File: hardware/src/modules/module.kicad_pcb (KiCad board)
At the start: 2 copper layers, 58 x 33.4 mm, 150 parts, among them J1 CONN_01X06, J5 CONN_01X06, U1 VL53L1X

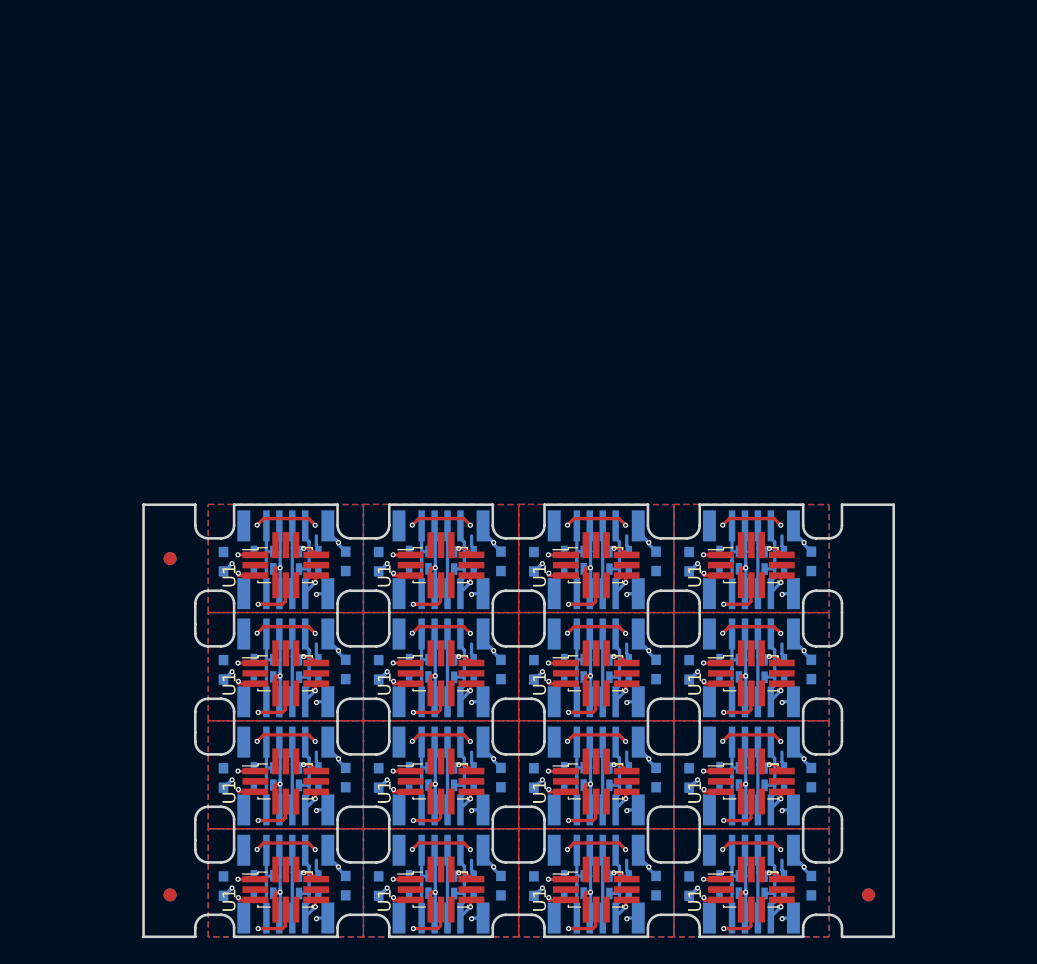
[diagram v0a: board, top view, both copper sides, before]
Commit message: fixed manufactury requirements
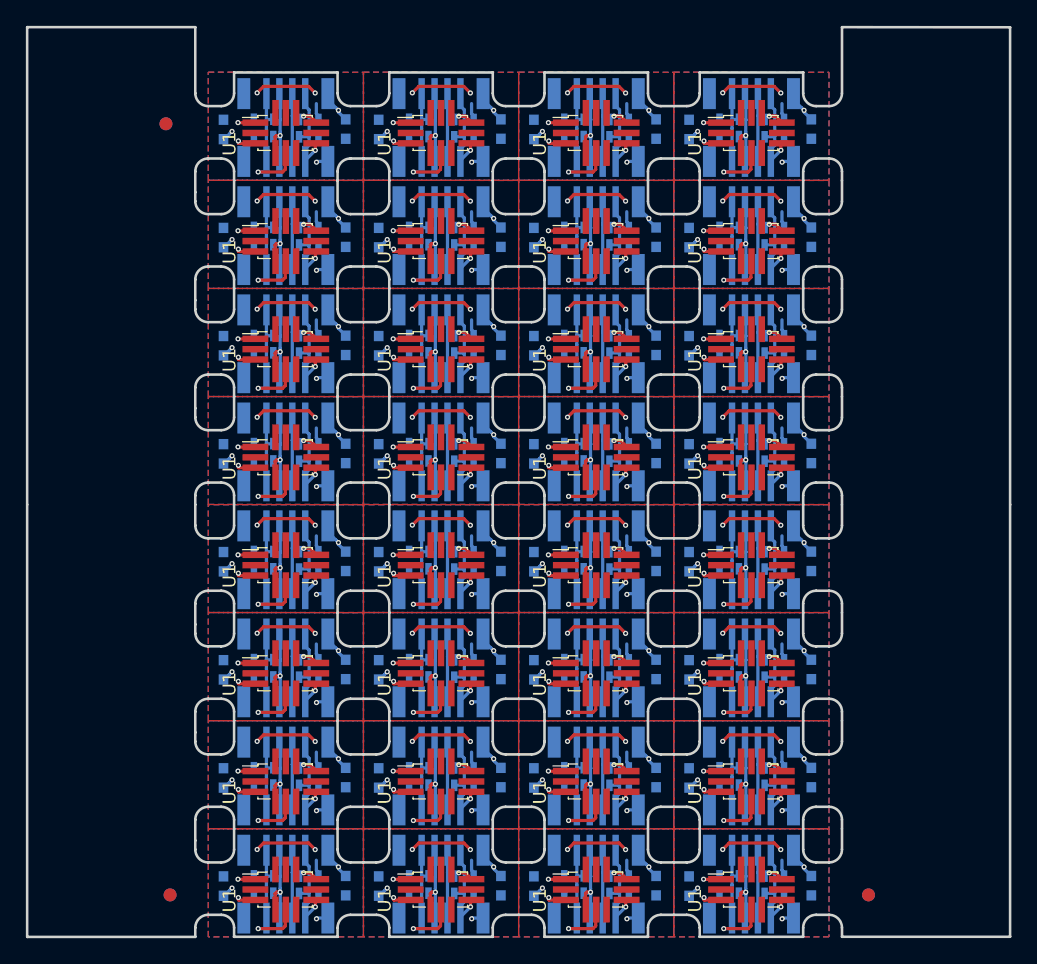
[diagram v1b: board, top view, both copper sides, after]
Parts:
- added C1: 100n, Capacitors_SMD:C_0603, B.Cu at (107.1, 66.9)
- added C1: 100n, Capacitors_SMD:C_0603, B.Cu at (143.1, 50.2)
- added C1: 100n, Capacitors_SMD:C_0603, B.Cu at (131.1, 50.2)
- added C1: 100n, Capacitors_SMD:C_0603, B.Cu at (119.1, 41.8)
- added C1: 100n, Capacitors_SMD:C_0603, B.Cu at (143.1, 66.9)
- added C1: 100n, Capacitors_SMD:C_0603, B.Cu at (143.1, 41.8)
- added C1: 100n, Capacitors_SMD:C_0603, B.Cu at (119.1, 66.9)
- added C1: 100n, Capacitors_SMD:C_0603, B.Cu at (131.1, 66.9)
- added C1: 100n, Capacitors_SMD:C_0603, B.Cu at (107.1, 58.5)
- added C1: 100n, Capacitors_SMD:C_0603, B.Cu at (107.1, 41.8)
- added C1: 100n, Capacitors_SMD:C_0603, B.Cu at (119.1, 58.5)
- added C1: 100n, Capacitors_SMD:C_0603, B.Cu at (131.1, 58.5)
- added C1: 100n, Capacitors_SMD:C_0603, B.Cu at (131.1, 41.8)
- added C1: 100n, Capacitors_SMD:C_0603, B.Cu at (119.1, 50.2)
- added C1: 100n, Capacitors_SMD:C_0603, B.Cu at (143.1, 58.5)
- added C1: 100n, Capacitors_SMD:C_0603, B.Cu at (107.1, 50.2)
- added C2: 4.7u, Capacitors_SMD:C_0603, B.Cu at (128.6, 41.8)
- added C2: 4.7u, Capacitors_SMD:C_0603, B.Cu at (152.6, 41.8)
- added C2: 4.7u, Capacitors_SMD:C_0603, B.Cu at (152.6, 58.5)
- added C2: 4.7u, Capacitors_SMD:C_0603, B.Cu at (152.6, 50.2)
- added C2: 4.7u, Capacitors_SMD:C_0603, B.Cu at (116.6, 66.9)
- added C2: 4.7u, Capacitors_SMD:C_0603, B.Cu at (152.6, 66.9)
- added C2: 4.7u, Capacitors_SMD:C_0603, B.Cu at (140.6, 66.9)
- added C2: 4.7u, Capacitors_SMD:C_0603, B.Cu at (128.6, 66.9)
- added C2: 4.7u, Capacitors_SMD:C_0603, B.Cu at (140.6, 50.2)
- added C2: 4.7u, Capacitors_SMD:C_0603, B.Cu at (128.6, 58.5)
- added C2: 4.7u, Capacitors_SMD:C_0603, B.Cu at (116.6, 41.8)
- added C2: 4.7u, Capacitors_SMD:C_0603, B.Cu at (116.6, 50.2)
- added C2: 4.7u, Capacitors_SMD:C_0603, B.Cu at (116.6, 58.5)
- added C2: 4.7u, Capacitors_SMD:C_0603, B.Cu at (128.6, 50.2)
- added C2: 4.7u, Capacitors_SMD:C_0603, B.Cu at (140.6, 58.5)
- added C2: 4.7u, Capacitors_SMD:C_0603, B.Cu at (140.6, 41.8)
- added J1: CONN_01X06, custom-footprints:CONN_Module, B.Cu at (112.0, 70.1)
- added J1: CONN_01X06, custom-footprints:CONN_Module, B.Cu at (147.9, 45.0)
- added J1: CONN_01X06, custom-footprints:CONN_Module, B.Cu at (135.9, 53.4)
- added J1: CONN_01X06, custom-footprints:CONN_Module, B.Cu at (124.0, 45.0)
- added J1: CONN_01X06, custom-footprints:CONN_Module, B.Cu at (135.9, 45.0)
- added J1: CONN_01X06, custom-footprints:CONN_Module, B.Cu at (135.9, 61.7)
- added J1: CONN_01X06, custom-footprints:CONN_Module, B.Cu at (135.9, 70.1)
- added J1: CONN_01X06, custom-footprints:CONN_Module, B.Cu at (112.0, 45.0)
- added J1: CONN_01X06, custom-footprints:CONN_Module, B.Cu at (147.9, 61.7)
- added J1: CONN_01X06, custom-footprints:CONN_Module, B.Cu at (124.0, 53.4)
- added J1: CONN_01X06, custom-footprints:CONN_Module, B.Cu at (147.9, 70.1)
- added J1: CONN_01X06, custom-footprints:CONN_Module, B.Cu at (124.0, 61.7)
- added J1: CONN_01X06, custom-footprints:CONN_Module, B.Cu at (124.0, 70.1)
- added J1: CONN_01X06, custom-footprints:CONN_Module, B.Cu at (112.0, 53.4)
- added J1: CONN_01X06, custom-footprints:CONN_Module, B.Cu at (147.9, 53.4)
- added J1: CONN_01X06, custom-footprints:CONN_Module, B.Cu at (112.0, 61.7)
- added J5: CONN_01X06, custom-footprints:CONN_Module, B.Cu at (124.0, 56.5)
- added J5: CONN_01X06, custom-footprints:CONN_Module, B.Cu at (112.0, 39.8)
- added J5: CONN_01X06, custom-footprints:CONN_Module, B.Cu at (135.9, 39.8)
- added J5: CONN_01X06, custom-footprints:CONN_Module, B.Cu at (147.9, 56.5)
- added J5: CONN_01X06, custom-footprints:CONN_Module, B.Cu at (147.9, 39.8)
- added J5: CONN_01X06, custom-footprints:CONN_Module, B.Cu at (112.0, 48.1)
- added J5: CONN_01X06, custom-footprints:CONN_Module, B.Cu at (124.0, 48.1)
- added J5: CONN_01X06, custom-footprints:CONN_Module, B.Cu at (135.9, 48.1)
- added J5: CONN_01X06, custom-footprints:CONN_Module, B.Cu at (124.0, 64.8)
- added J5: CONN_01X06, custom-footprints:CONN_Module, B.Cu at (135.9, 64.8)
- added J5: CONN_01X06, custom-footprints:CONN_Module, B.Cu at (112.0, 56.5)
- added J5: CONN_01X06, custom-footprints:CONN_Module, B.Cu at (135.9, 56.5)
- added J5: CONN_01X06, custom-footprints:CONN_Module, B.Cu at (147.9, 64.8)
- added J5: CONN_01X06, custom-footprints:CONN_Module, B.Cu at (112.0, 64.8)
- added J5: CONN_01X06, custom-footprints:CONN_Module, B.Cu at (147.9, 48.1)
- added J5: CONN_01X06, custom-footprints:CONN_Module, B.Cu at (124.0, 39.8)
- added R5: 10k, Resistors_SMD:R_0603, B.Cu at (146.2, 57.8)
- added R5: 10k, Resistors_SMD:R_0603, B.Cu at (146.2, 49.4)
- added R5: 10k, Resistors_SMD:R_0603, B.Cu at (122.2, 41.0)
- added R5: 10k, Resistors_SMD:R_0603, B.Cu at (134.2, 41.0)
- added R5: 10k, Resistors_SMD:R_0603, B.Cu at (134.2, 57.8)
- added R5: 10k, Resistors_SMD:R_0603, B.Cu at (134.2, 49.4)
- added R5: 10k, Resistors_SMD:R_0603, B.Cu at (110.2, 41.0)
- added R5: 10k, Resistors_SMD:R_0603, B.Cu at (110.2, 66.1)
- added R5: 10k, Resistors_SMD:R_0603, B.Cu at (122.2, 66.1)
- added R5: 10k, Resistors_SMD:R_0603, B.Cu at (122.2, 49.4)
- added R5: 10k, Resistors_SMD:R_0603, B.Cu at (146.2, 41.0)
- added R5: 10k, Resistors_SMD:R_0603, B.Cu at (134.2, 66.1)
- added R5: 10k, Resistors_SMD:R_0603, B.Cu at (110.2, 49.4)
- added R5: 10k, Resistors_SMD:R_0603, B.Cu at (146.2, 66.1)
- added R5: 10k, Resistors_SMD:R_0603, B.Cu at (110.2, 57.8)
- added R5: 10k, Resistors_SMD:R_0603, B.Cu at (122.2, 57.8)
- added R6: 10k, Resistors_SMD:R_0603, B.Cu at (146.2, 67.5)
- added R6: 10k, Resistors_SMD:R_0603, B.Cu at (134.2, 50.7)
- added R6: 10k, Resistors_SMD:R_0603, B.Cu at (110.2, 59.1)
- added R6: 10k, Resistors_SMD:R_0603, B.Cu at (110.2, 50.7)
- added R6: 10k, Resistors_SMD:R_0603, B.Cu at (122.2, 59.1)
- added R6: 10k, Resistors_SMD:R_0603, B.Cu at (134.2, 59.1)
- added R6: 10k, Resistors_SMD:R_0603, B.Cu at (146.2, 59.1)
- added R6: 10k, Resistors_SMD:R_0603, B.Cu at (146.2, 42.4)
- added R6: 10k, Resistors_SMD:R_0603, B.Cu at (122.2, 67.5)
- added R6: 10k, Resistors_SMD:R_0603, B.Cu at (134.2, 67.5)
- added R6: 10k, Resistors_SMD:R_0603, B.Cu at (110.2, 67.5)
- added R6: 10k, Resistors_SMD:R_0603, B.Cu at (122.2, 50.7)
- added R6: 10k, Resistors_SMD:R_0603, B.Cu at (134.2, 42.4)
- added R6: 10k, Resistors_SMD:R_0603, B.Cu at (146.2, 50.7)
- added R6: 10k, Resistors_SMD:R_0603, B.Cu at (122.2, 42.4)
- added R6: 10k, Resistors_SMD:R_0603, B.Cu at (110.2, 42.4)
- added R7: 10k, Resistors_SMD:R_0603, B.Cu at (113.7, 66.1)
- added R7: 10k, Resistors_SMD:R_0603, B.Cu at (113.7, 49.4)
- added R7: 10k, Resistors_SMD:R_0603, B.Cu at (149.7, 49.4)
- added R7: 10k, Resistors_SMD:R_0603, B.Cu at (113.7, 41.1)
- added R7: 10k, Resistors_SMD:R_0603, B.Cu at (125.7, 41.1)
- added R7: 10k, Resistors_SMD:R_0603, B.Cu at (137.7, 41.1)
- added R7: 10k, Resistors_SMD:R_0603, B.Cu at (149.7, 41.1)
- added R7: 10k, Resistors_SMD:R_0603, B.Cu at (137.7, 49.4)
- added R7: 10k, Resistors_SMD:R_0603, B.Cu at (149.7, 66.1)
- added R7: 10k, Resistors_SMD:R_0603, B.Cu at (125.7, 49.4)
- added R7: 10k, Resistors_SMD:R_0603, B.Cu at (125.7, 66.1)
- added R7: 10k, Resistors_SMD:R_0603, B.Cu at (149.7, 57.8)
- added R7: 10k, Resistors_SMD:R_0603, B.Cu at (137.7, 57.8)
- added R7: 10k, Resistors_SMD:R_0603, B.Cu at (137.7, 66.1)
- added R7: 10k, Resistors_SMD:R_0603, B.Cu at (125.7, 57.8)
- added R7: 10k, Resistors_SMD:R_0603, B.Cu at (113.7, 57.8)
- added R8: 10k, Resistors_SMD:R_0603, B.Cu at (113.7, 67.5)
- added R8: 10k, Resistors_SMD:R_0603, B.Cu at (137.7, 50.8)
- added R8: 10k, Resistors_SMD:R_0603, B.Cu at (149.7, 67.5)
- added R8: 10k, Resistors_SMD:R_0603, B.Cu at (125.7, 59.1)
- added R8: 10k, Resistors_SMD:R_0603, B.Cu at (137.7, 59.1)
- added R8: 10k, Resistors_SMD:R_0603, B.Cu at (137.7, 42.4)
- added R8: 10k, Resistors_SMD:R_0603, B.Cu at (125.7, 42.4)
- added R8: 10k, Resistors_SMD:R_0603, B.Cu at (149.7, 42.4)
- added R8: 10k, Resistors_SMD:R_0603, B.Cu at (125.7, 67.5)
- added R8: 10k, Resistors_SMD:R_0603, B.Cu at (137.7, 67.5)
- added R8: 10k, Resistors_SMD:R_0603, B.Cu at (149.7, 50.8)
- added R8: 10k, Resistors_SMD:R_0603, B.Cu at (149.7, 59.1)
- added R8: 10k, Resistors_SMD:R_0603, B.Cu at (113.7, 50.8)
- added R8: 10k, Resistors_SMD:R_0603, B.Cu at (113.7, 42.4)
- added R8: 10k, Resistors_SMD:R_0603, B.Cu at (113.7, 59.1)
- added R8: 10k, Resistors_SMD:R_0603, B.Cu at (125.7, 50.8)
- added U1: VL53L1X, custom-footprints:ST_VL53L_HandSoldering, F.Cu at (135.9, 50.5)
- added U1: VL53L1X, custom-footprints:ST_VL53L_HandSoldering, F.Cu at (147.9, 42.1)
- added U1: VL53L1X, custom-footprints:ST_VL53L_HandSoldering, F.Cu at (124.0, 58.9)
- added U1: VL53L1X, custom-footprints:ST_VL53L_HandSoldering, F.Cu at (124.0, 67.2)
- added U1: VL53L1X, custom-footprints:ST_VL53L_HandSoldering, F.Cu at (135.9, 67.2)
- added U1: VL53L1X, custom-footprints:ST_VL53L_HandSoldering, F.Cu at (147.9, 67.2)
- added U1: VL53L1X, custom-footprints:ST_VL53L_HandSoldering, F.Cu at (112.0, 58.9)
- added U1: VL53L1X, custom-footprints:ST_VL53L_HandSoldering, F.Cu at (112.0, 67.2)
- added U1: VL53L1X, custom-footprints:ST_VL53L_HandSoldering, F.Cu at (147.9, 50.5)
- added U1: VL53L1X, custom-footprints:ST_VL53L_HandSoldering, F.Cu at (135.9, 58.9)
- added U1: VL53L1X, custom-footprints:ST_VL53L_HandSoldering, F.Cu at (112.0, 42.1)
- added U1: VL53L1X, custom-footprints:ST_VL53L_HandSoldering, F.Cu at (147.9, 58.9)
- added U1: VL53L1X, custom-footprints:ST_VL53L_HandSoldering, F.Cu at (135.9, 42.1)
- added U1: VL53L1X, custom-footprints:ST_VL53L_HandSoldering, F.Cu at (112.0, 50.5)
- added U1: VL53L1X, custom-footprints:ST_VL53L_HandSoldering, F.Cu at (124.0, 50.5)
- added U1: VL53L1X, custom-footprints:ST_VL53L_HandSoldering, F.Cu at (124.0, 42.1)
- moved REF** 33.6 mm to (102.7, 41.4) (x2)
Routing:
- net Net-(J1-Pad2): track 166.8 -> 333.7 mm, vias 16 -> 32
- net /VDD_1M: track 143.9 -> 287.9 mm, vias 64 -> 128
- net Net-(J1-Pad5): track 128.8 -> 257.7 mm, vias 16 -> 32
- net Net-(J1-Pad3): track 121.0 -> 241.9 mm, vias 16 -> 32
- net Net-(J1-Pad4): track 117.1 -> 234.3 mm, vias 16 -> 32
- net /GND_1M: track 73.0 -> 146.1 mm, vias 48 -> 96
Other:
- board size 58 x 33.4 mm -> 76 x 70.3 mm
